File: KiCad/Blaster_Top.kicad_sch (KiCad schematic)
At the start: 28 parts, among them Q4 BUK9832-55A, Q5 BUK9832-55A, SW2 Fire, SW3 Freq Select, SW4 Fire Select, U3 PIC16F1788-IP, U4 Audio Board

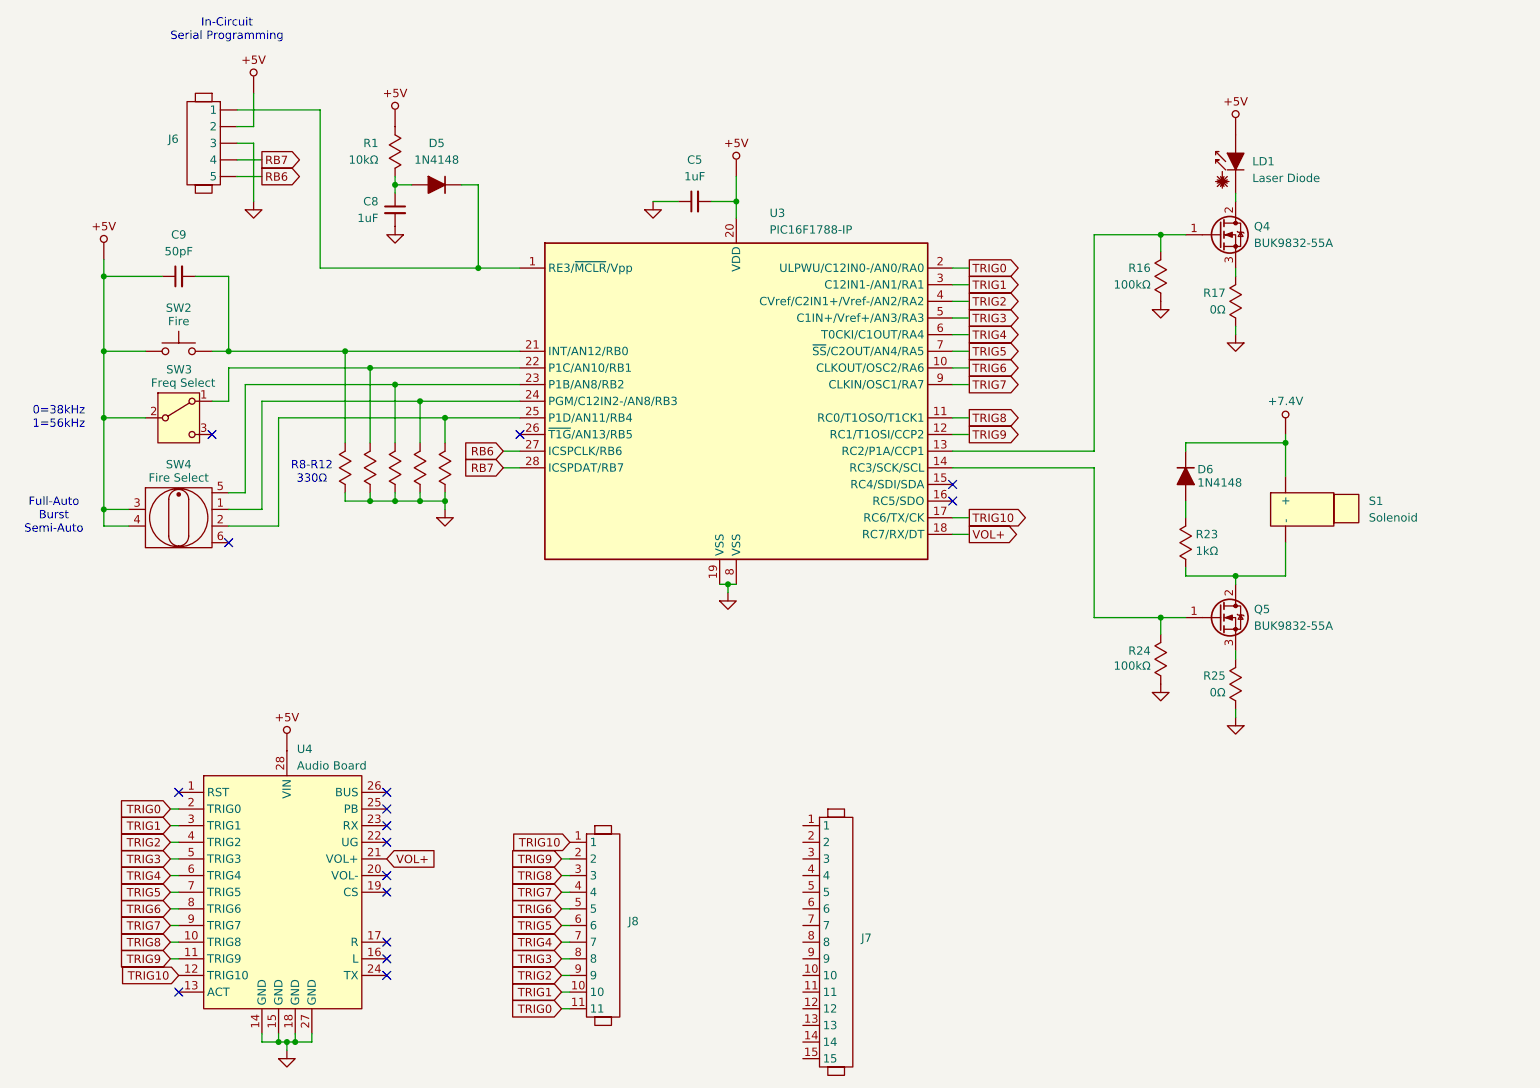
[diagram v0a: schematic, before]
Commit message: fixed the schematics, and got the new components added into the PCB, need to rerun a lot of traces.
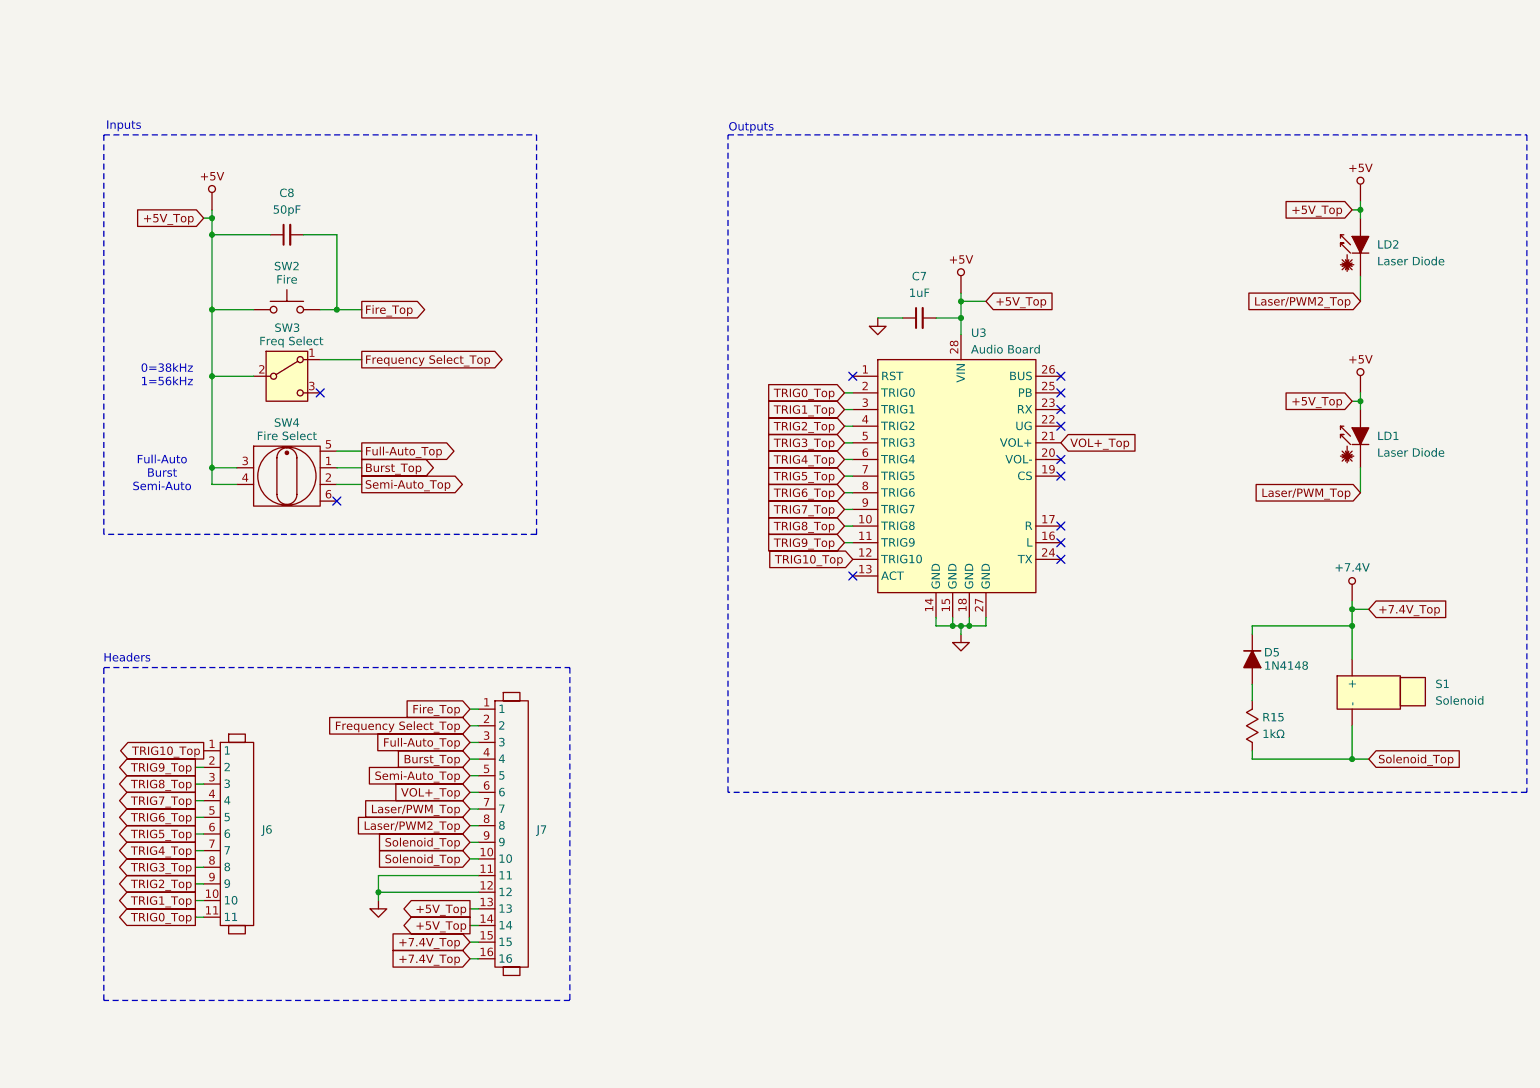
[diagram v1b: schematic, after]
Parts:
- removed C5, C8: 1uF, Capacitor_SMD:C_0805_2012Metric_Pad1.18x1.45mm_HandSolder, symbol Device:C_Small
- removed D5: 1N4148, Diode_SMD:D_0805_2012Metric_Pad1.15x1.40mm_HandSolder, symbol Device:D_Filled
- removed J6: ~, Connector_PinHeader_2.54mm:PinHeader_1x05_P2.54mm_Vertical, symbol Libraries:Header_1x5
- removed J7: ~, symbol Libraries:Header_1x15
- removed Q4, Q5: BUK9832-55A, Package_TO_SOT_SMD:SOT-223-3_TabPin2, symbol Transistor_FET:BUK7880-55A
- removed R1: 10kΩ, Resistor_SMD:R_0805_2012Metric_Pad1.20x1.40mm_HandSolder, symbol Libraries:R_Custom
- removed R16, R24: 100kΩ, Resistor_SMD:R_0805_2012Metric_Pad1.20x1.40mm_HandSolder, symbol Libraries:R_Custom
- removed R17, R25: 0Ω, Resistor_SMD:R_0805_2012Metric_Pad1.20x1.40mm_HandSolder, symbol Libraries:R_Custom
- removed R18, R19, R20, R21, R22: 330Ω, Resistor_SMD:R_0805_2012Metric_Pad1.20x1.40mm_HandSolder, symbol Libraries:R_Custom
- removed U3: PIC16F1788-IP, AlexWheelockFootprintLibrary:SSOP-28, symbol Libraries:PIC16F883_BIN_ACOUT
- added C7: 1uF, Capacitor_SMD:C_0805_2012Metric_Pad1.18x1.45mm_HandSolder, symbol Device:C_Small
- added J7: ~, Connector_PinHeader_2.54mm:PinHeader_1x16_P2.54mm_Vertical, symbol Libraries:Header_1x16
- added LD2: Laser Diode, AlexWheelockFootprintLibrary:Project_Locking_Output_Header, symbol Libraries:Laser_Diode
- J6: renamed from J8; footprint (none) -> Connector_PinHeader_2.54mm:PinHeader_1x11_P2.54mm_Vertical
- renumbered C9 to C8, D6 to D5, R23 to R15, U4 to U3
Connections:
- net +5V: now also C7.2, J7.13, J7.14, LD2.1 (A)
- net Laser/PWM_Top: now reaches LD1.2 (K)
- net Laser/PWM_Top: now also J7.7
- net Fire_Top: now reaches C8.2, SW2.2
- net Fire_Top: now also J7.1
- net Solenoid_Top: now reaches R15.1, S1.2 (-)
- net Solenoid_Top: now also J7.10, J7.9
- net Frequency Select_Top: now reaches SW3.1 (A)
- net Frequency Select_Top: now also J7.2
- net Burst_Top: now reaches SW4.1
- net Burst_Top: now also J7.4
- net +7.4V_Top: now reaches D5.1 (K), S1.1 (+)
- net +7.4V_Top: now also J7.15, J7.16
- net Full-Auto_Top: now reaches SW4.5
- net Full-Auto_Top: now also J7.3
- net Semi-Auto_Top: now reaches SW4.2
- net Semi-Auto_Top: now also J7.5
- net TRIG0 renamed TRIG0_Top
- net TRIG1 renamed TRIG1_Top
- net TRIG10 renamed TRIG10_Top
- net TRIG2 renamed TRIG2_Top
- net TRIG3 renamed TRIG3_Top
- net TRIG4 renamed TRIG4_Top
- net TRIG5 renamed TRIG5_Top
- net TRIG6 renamed TRIG6_Top
- net TRIG7 renamed TRIG7_Top
- net TRIG8 renamed TRIG8_Top
- net TRIG9 renamed TRIG9_Top
- net VOL+ renamed VOL+_Top
- net VOL+_Top: now also J7.6
- new net: J7.11, J7.12
- new net Laser/PWM2_Top: J7.8, LD2.2 (K)
- no-connect marks 16 -> 13
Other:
- note added: "Headers"
- note added: "Inputs"
- note added: "Outputs"
- note removed: "In-Circuit Serial Programming"
- note removed: "R8-R12 330Ω"
- company: (none) -> Idaho State University
- title: (none) -> Blaster Top
- moved on the sheet: C8, D5, J6, LD1, R15, S1, SW2, SW3, SW4, U3

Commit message: finished blaster PCB
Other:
- moved on the sheet: C7, C8, D5, J6, J7, LD1, LD2, R15, S1, SW2, SW3, SW4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

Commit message: updated blaster schematic
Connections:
- net +7.4V_Top renamed +12V_Top
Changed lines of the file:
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@@
 		)
 	)
-	(global_label "+7.4V_Top"
+	(global_label "+12V_Top"
 		(shape input)
 		(at 226.06 113.03 0)
@@
 		)
 		(property "Intersheetrefs" "${INTERSHEET_REFS}"
-			(at 238.9632 113.03 0)
+			(at 238.3584 113.03 0)
 			(effects
 				(font
@@
 		)
 	)
-	(global_label "+7.4V_Top"
+	(global_label "+12V_Top"
 		(shape input)
 		(at 90.17 163.83 180)
@@
 		)
 		(property "Intersheetrefs" "${INTERSHEET_REFS}"
-			(at 77.2668 163.83 0)
+			(at 77.8716 163.83 0)
 			(effects
 				(font
@@
 		)
 	)
-	(global_label "+7.4V_Top"
+	(global_label "+12V_Top"
 		(shape input)
 		(at 90.17 166.37 180)
@@
 		)
 		(property "Intersheetrefs" "${INTERSHEET_REFS}"
-			(at 77.2668 166.37 0)
+			(at 77.8716 166.37 0)
 			(effects
 				(font
@@
 			)
 		)
-		(property "Value" "+7.4V"
+		(property "Value" "+12V"
 			(at 223.52 106.68 0)
 			(effects
